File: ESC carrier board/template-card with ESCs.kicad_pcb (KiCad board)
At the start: 2 copper layers, 111.8 x 83 mm, 13 parts, among them J1 Conn_01x10_Pin, J3 Conn_01x04_Pin, J4 Conn_01x04_Pin, J5 Conn_01x04_Pin, SW1 SW_DPDT_x2, U2 ESC, U4 ESC, U6 ESC

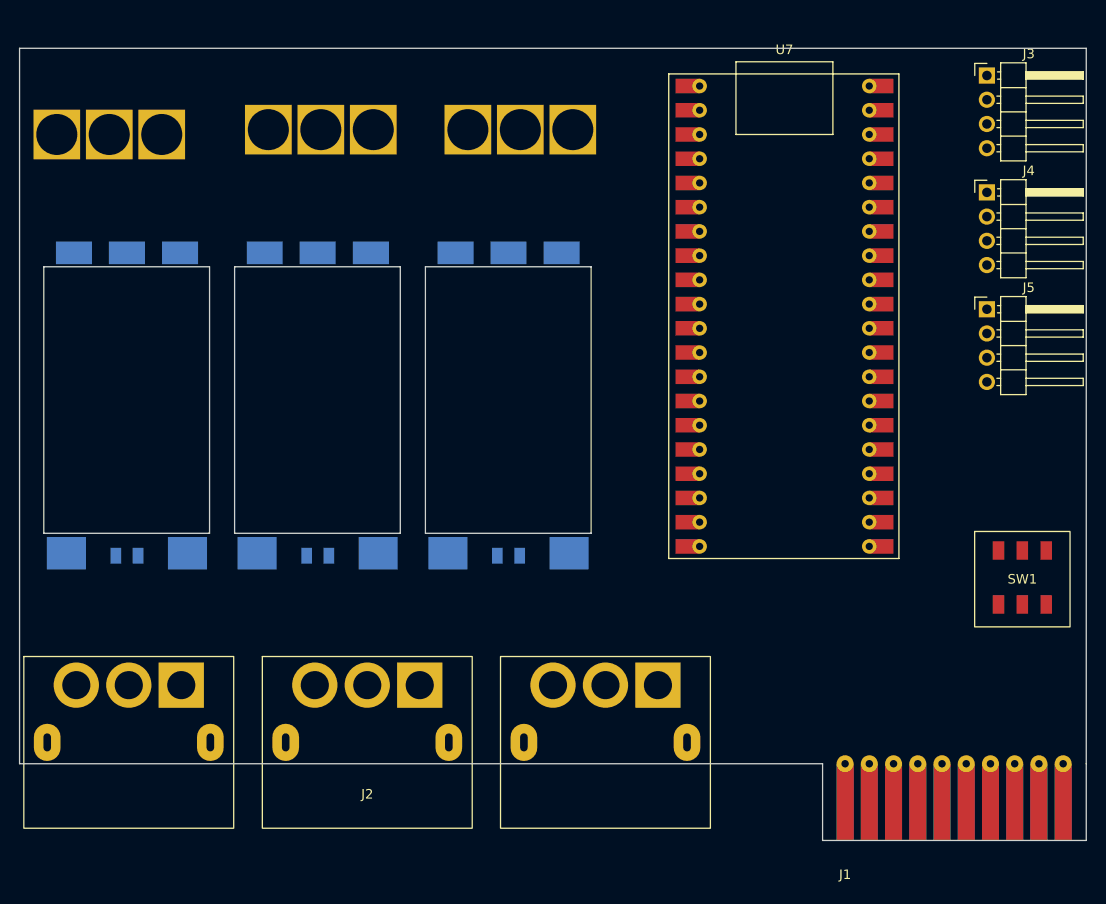
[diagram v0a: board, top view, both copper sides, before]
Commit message: Routed board
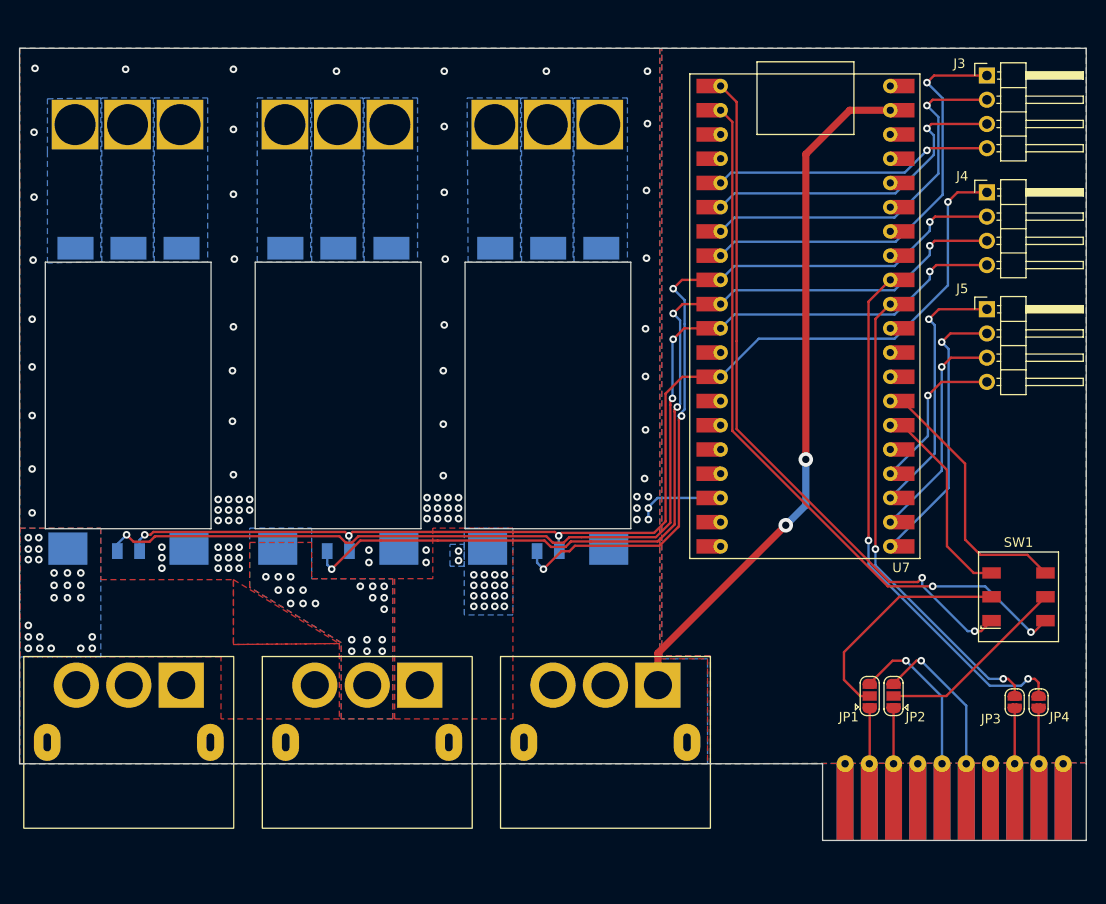
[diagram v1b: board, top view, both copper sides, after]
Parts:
- added JP1: Jumper_3_Open, Jumper:SolderJumper-3_P1.3mm_Open_RoundedPad1.0x1.5mm, F.Cu at (174.8, 92.9)
- added JP2: Jumper_3_Open, Jumper:SolderJumper-3_P1.3mm_Open_RoundedPad1.0x1.5mm, F.Cu at (177.3, 92.9)
- added JP3: Jumper_2_Bridged, Jumper:SolderJumper-2_P1.3mm_Open_RoundedPad1.0x1.5mm, F.Cu at (190.0, 93.5)
- added JP4: Jumper_2_Bridged, Jumper:SolderJumper-2_P1.3mm_Open_RoundedPad1.0x1.5mm, F.Cu at (192.5, 93.5)
- J1: value Conn_01x10_Pin -> ~
- SW1: footprint 2024-backplane:SW_CUI_DPDT -> Kelpie_Default:CUI-Switch-SMD
- U1, U3, U5: footprint ESC-Thruster:MR60-F -> 2024-backplane:MR60-F
- U7: footprint ESC-carrier:ESP32-S3-Pico -> Kelpie_Default:ESP32-S3-Pico
- moved U6 4.19 mm to (132.7, 79.1)
- moved U5 2.87 mm to (141.0, 33.0)
- moved U4 2.21 mm to (110.7, 79.1)
- moved U7 2.20 mm to (169.3, 44.2)
- moved U1 2.18 mm to (97.0, 33.0)
- moved SW1 1.89 mm to (190.4, 82.5), turned to 90 degrees
- moved U3 1.82 mm to (119.0, 33.0)
- moved U2 0.51 mm to (88.7, 79.1)
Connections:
- net GND1 renamed sGND
- J1 pad 2: /tx0/sda0 -> Net-(J1-TX0/SDA0)
- J1 pad 3: /rx0/scl0 -> Net-(J1-RX0/SCL0)
- J1 pad 5: /tx1/sda1 -> Net-(J1-TX1/SDA1)
- J1 pad 6: /rx1/scl1 -> Net-(J1-RX1/SCL1)
- J1 pad 8: /tx2/sda2 -> Net-(J1-TX2/SDA2)
- J1 pad 9: /rx2/scl2 -> Net-(J1-RX2/SCL2)
- J2 pad : (no net) -> GND
- J2 pad 1: /48v -> unconnected-(J2A-48V-Pad1)
- J2 pad 7: /24v -> unconnected-(J2C-24V-Pad7)
- SW1 pad 1: /tx -> TX0
- SW1 pad 2: /tx0/sda0 -> Net-(JP1-C)
- SW1 pad 3: /sda -> SDA0
- SW1 pad 4: /rx -> RX0
- SW1 pad 5: /rx0/scl0 -> Net-(JP2-C)
- SW1 pad 6: /scl -> SCL0
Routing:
- net /sg: track 0.00 -> 120.7 mm, vias 0 -> 4
- net /sGP8: track 0.00 -> 116.0 mm, vias 0 -> 4
- net /sGP7: track 0.00 -> 98.5 mm, vias 0 -> 4
- net /sGP6: track 0.00 -> 79.7 mm, vias 0 -> 4
- net RX0: track 0.00 -> 76.2 mm, vias 0 -> 2
- net TX0: track 0.00 -> 73.5 mm, vias 0 -> 2
- net /5v: track 0.00 -> 72.8 mm, vias 0 -> 2
- net SCL1: track 0.00 -> 55.7 mm, vias 0 -> 2
- net SDA1: track 0.00 -> 48.9 mm, vias 0 -> 2
- net Net-(J3-Pin_1): track 0.00 -> 44.9 mm, vias 0 -> 1
- net Net-(J3-Pin_2): track 0.00 -> 39.5 mm, vias 0 -> 1
- net Net-(J3-Pin_3): track 0.00 -> 34.2 mm, vias 0 -> 1
- net Net-(J3-Pin_4): track 0.00 -> 29.4 mm, vias 0 -> 1
- net Net-(J5-Pin_2): track 0.00 -> 29.4 mm, vias 0 -> 1
- net Net-(J5-Pin_1): track 0.00 -> 27.4 mm, vias 0 -> 1
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- added copper zone on B.Cu, net /12v1
- added copper zone on F.Cu, net /12v1
- added copper zone on B.Cu, net /12v2
- added copper zone on F.Cu, net /12v2
- added copper zone on B.Cu, net /12v3
- added copper zone on F.Cu, net /12v3
- added copper zone on B.Cu, net GND
- added copper zone on F.Cu, net GND
- added copper zone on B.Cu, net Net-(U1-A)
- added copper zone on B.Cu, net Net-(U1-B)
- added copper zone on B.Cu, net Net-(U1-C)
- added copper zone on B.Cu, net Net-(U3-A)
- added copper zone on B.Cu, net Net-(U3-B)
- added copper zone on B.Cu, net Net-(U3-C)
- added copper zone on B.Cu, net Net-(U5-A)
- added copper zone on B.Cu, net Net-(U5-B)
- added copper zone on B.Cu, net Net-(U5-C)
- added copper zone on B.Cu, net sGND
- added copper zone on F.Cu, net sGND
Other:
- outline, holes or cut-outs redrawn

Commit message: Modified board and footprints
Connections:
- J3 pad 1: Net-(J3-Pin_1) -> sGND
- J4 pad 1: /sg -> sGND
- J5 pad 1: Net-(J5-Pin_1) -> sGND
- U2 pad G: /sg -> sGND
- U4 pad G: /sg -> sGND
- U6 pad G: /sg -> sGND
- U7 pad 13: /sg -> sGND
- U7 pad 23: Net-(J5-Pin_1) -> sGND
- U7 pad 28: unconnected-(U7-GND-Pad28) -> sGND
- U7 pad 3: unconnected-(U7-GND-Pad3) -> sGND
- U7 pad 33: unconnected-(U7-GND-Pad33) -> sGND
- U7 pad 38: unconnected-(U7-GND-Pad38) -> sGND
- U7 pad 8: Net-(J3-Pin_1) -> sGND
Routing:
- net /sg: track 120.7 -> 0.00 mm, vias 4 -> 0
- net sGND: track 0.00 -> 79.7 mm, vias 0 -> 43
- net Net-(J3-Pin_1): track 44.9 -> 0.00 mm, vias 1 -> 0
- net Net-(J5-Pin_1): track 27.4 -> 0.00 mm, vias 1 -> 0
- net Net-(J5-Pin_3): track 23.6 -> 24.8 mm
- net Net-(J5-Pin_2): track 29.4 -> 30.2 mm
- added copper zone on F.Cu, net Net-(U1-A)
- added copper zone on F.Cu, net Net-(U1-B)
- added copper zone on F.Cu, net Net-(U1-C)
- added copper zone on F.Cu, net Net-(U3-A)
- added copper zone on F.Cu, net Net-(U3-B)
- added copper zone on F.Cu, net Net-(U3-C)
- added copper zone on F.Cu, net Net-(U5-A)
- added copper zone on F.Cu, net Net-(U5-B)
- added copper zone on F.Cu, net Net-(U5-C)

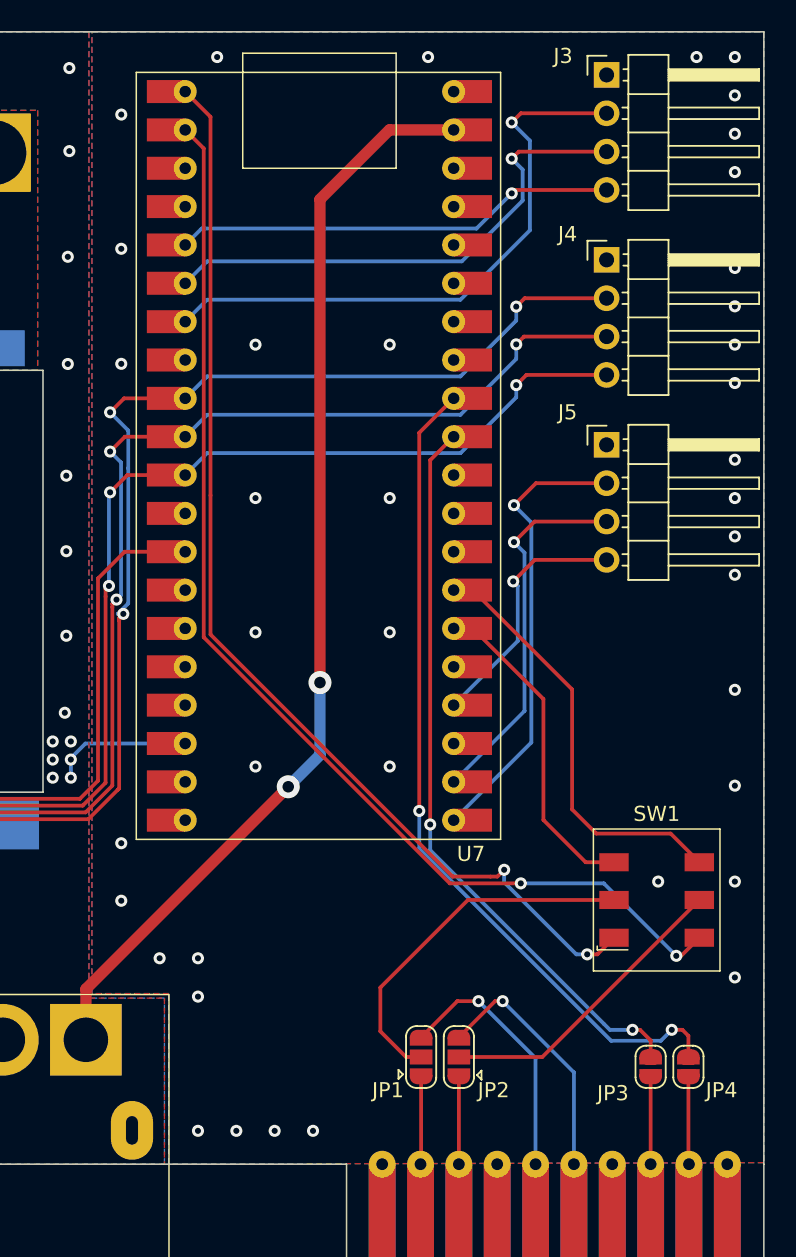
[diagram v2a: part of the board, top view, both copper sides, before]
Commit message: ESC carrier board jumper routing
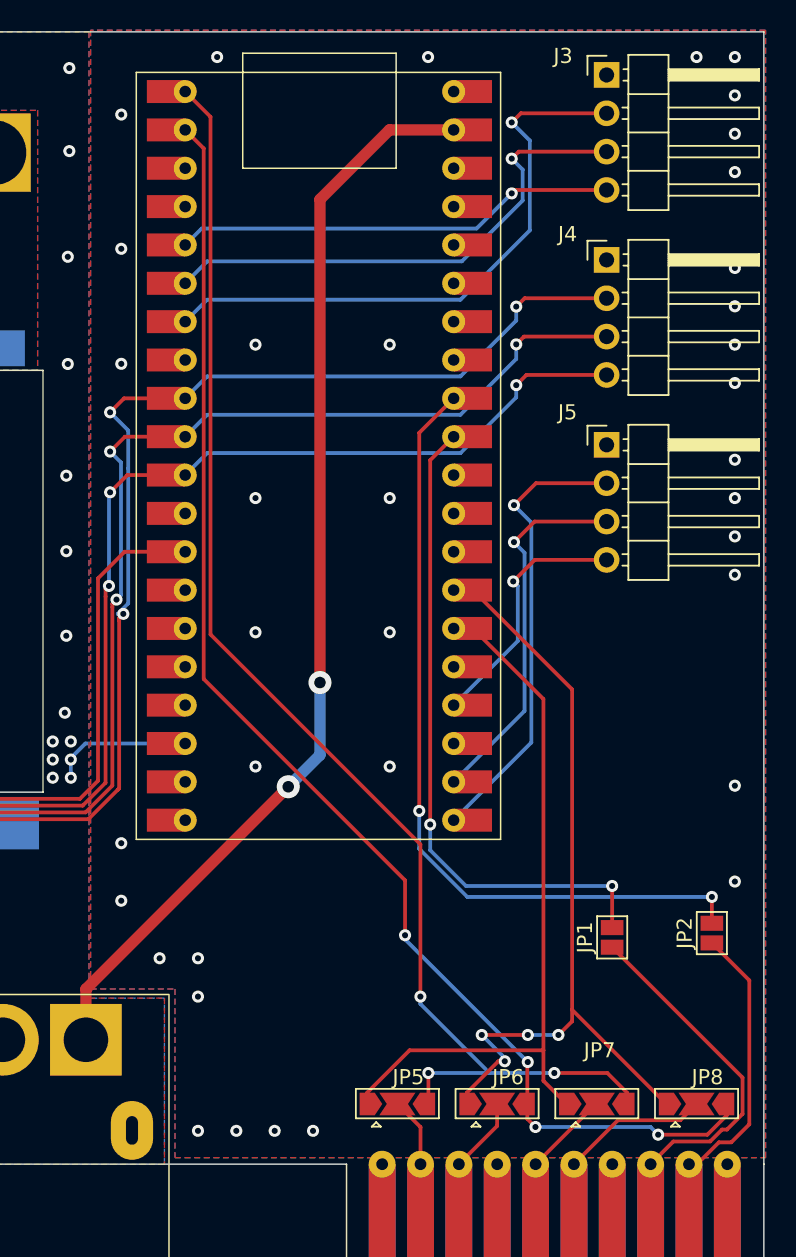
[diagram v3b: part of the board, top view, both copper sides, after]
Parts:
- removed JP3, JP4: Jumper_2_Bridged, Jumper:SolderJumper-2_P1.3mm_Open_RoundedPad1.0x1.5mm
- removed SW1: SW_DPDT_x2, Kelpie_Default:CUI-Switch-SMD
- added JP5: SolderJumper_3_Open, Jumper:SolderJumper-3_P2.0mm_Open_TrianglePad1.0x1.5mm, F.Cu at (173.2, 96.0)
- added JP6: SolderJumper_3_Open, Jumper:SolderJumper-3_P2.0mm_Open_TrianglePad1.0x1.5mm, F.Cu at (179.8, 96.0)
- added JP7: SolderJumper_3_Open, Jumper:SolderJumper-3_P2.0mm_Open_TrianglePad1.0x1.5mm, F.Cu at (186.4, 96.0)
- added JP8: SolderJumper_3_Open, Jumper:SolderJumper-3_P2.0mm_Open_TrianglePad1.0x1.5mm, F.Cu at (193.0, 96.0)
- JP1, JP2: value Jumper_3_Open -> SolderJumper_2_Open; footprint Jumper:SolderJumper-3_P1.3mm_Open_RoundedPad1.0x1.5mm -> Jumper:SolderJumper-2_P1.3mm_Open_Pad1.0x1.5mm
- moved JP2 18.7 mm to (194.1, 84.7)
- moved JP1 14.9 mm to (187.5, 85.0)
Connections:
- J1 pad 2: Net-(J1-TX0/SDA0) -> TX0/SDA0
- J1 pad 3: Net-(J1-RX0/SCL0) -> RX0/SCL0
- J1 pad 5: Net-(J1-TX1/SDA1) -> TX1/SDA1
- J1 pad 6: Net-(J1-RX1/SCL1) -> RX1/SCL1
- JP1 pad 1: Net-(J1-TX0/SDA0) -> Net-(J1-TX2/SDA2)
- JP1 pad 2: Net-(JP1-C) -> SDA1
- JP2 pad 1: Net-(J1-RX0/SCL0) -> Net-(J1-RX2/SCL2)
- JP2 pad 2: Net-(JP2-C) -> SCL1
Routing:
- net SDA0: track 20.5 -> 47.7 mm
- net SCL0: track 27.1 -> 53.0 mm, vias 0 -> 4
- net Net-(JP1-C): track 24.2 -> 0.00 mm
- net Net-(JP2-C): track 20.2 -> 0.00 mm
- net Net-(J1-TX1/SDA1): track 17.2 -> 0.00 mm, vias 1 -> 0
- net Net-(J1-RX1/SCL1): track 16.6 -> 0.00 mm, vias 1 -> 0
- net TX0: track 73.5 -> 89.9 mm, vias 2 -> 3
- net Net-(J1-TX2/SDA2): track 5.80 -> 22.1 mm
- net RX0: track 76.2 -> 89.8 mm, vias 2 -> 4
- net Net-(J1-RX2/SCL2): track 5.82 -> 18.6 mm
- net RX1/SCL1: track 0.00 -> 9.77 mm
- net Net-(J1-TX0/SDA0): track 5.82 -> 0.00 mm
- net Net-(J1-RX0/SCL0): track 5.80 -> 0.00 mm
- net TX1/SDA1: track 0.00 -> 5.71 mm
- net SDA1: track 48.9 -> 43.8 mm
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
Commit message: modified pcb
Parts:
- moved JP8 10.2 mm to (187.3, 87.6)
- moved JP1 8.89 mm to (190.5, 93.3)
- moved JP6 8.80 mm to (177.2, 87.6)
- moved JP2 8.70 mm to (193.0, 93.3)
- moved JP7 5.34 mm to (182.2, 92.7)
- moved JP5 3.53 mm to (172.0, 92.7)
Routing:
- net sGND: track 79.7 -> 97.7 mm, vias 40 -> 41
- net Net-(J1-TX2/SDA2): track 22.1 -> 6.75 mm
- net RX0: track 89.8 -> 76.3 mm, vias 4 -> 0
- net SCL0: track 53.0 -> 41.5 mm, vias 4 -> 3
- net Net-(J1-RX2/SCL2): track 18.6 -> 8.21 mm
- net RX0/SCL0: track 5.04 -> 12.4 mm
- net SDA1: track 43.8 -> 48.0 mm, vias 2 -> 0
- net SDA0: track 47.7 -> 43.7 mm, vias 0 -> 3
- net TX0/SDA0: track 4.68 -> 8.49 mm
- net TX0: track 89.9 -> 86.2 mm, vias 3 -> 2
- net SCL1: track 53.2 -> 49.5 mm, vias 2 -> 0
- net RX1/SCL1: track 9.77 -> 13.3 mm
- net TX1/SDA1: track 5.71 -> 7.35 mm
- net Net-(U5-C): vias 0 -> 6
- net Net-(U5-B): vias 0 -> 6
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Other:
- board text added: "0"
- board text added: "1"
- board text added: "2"
- board text added: "RX"
- board text added: "SCL"
- board text added: "SCL1"
- board text added: "SDA"
- board text added: "SDA1"
- board text added: "TX"

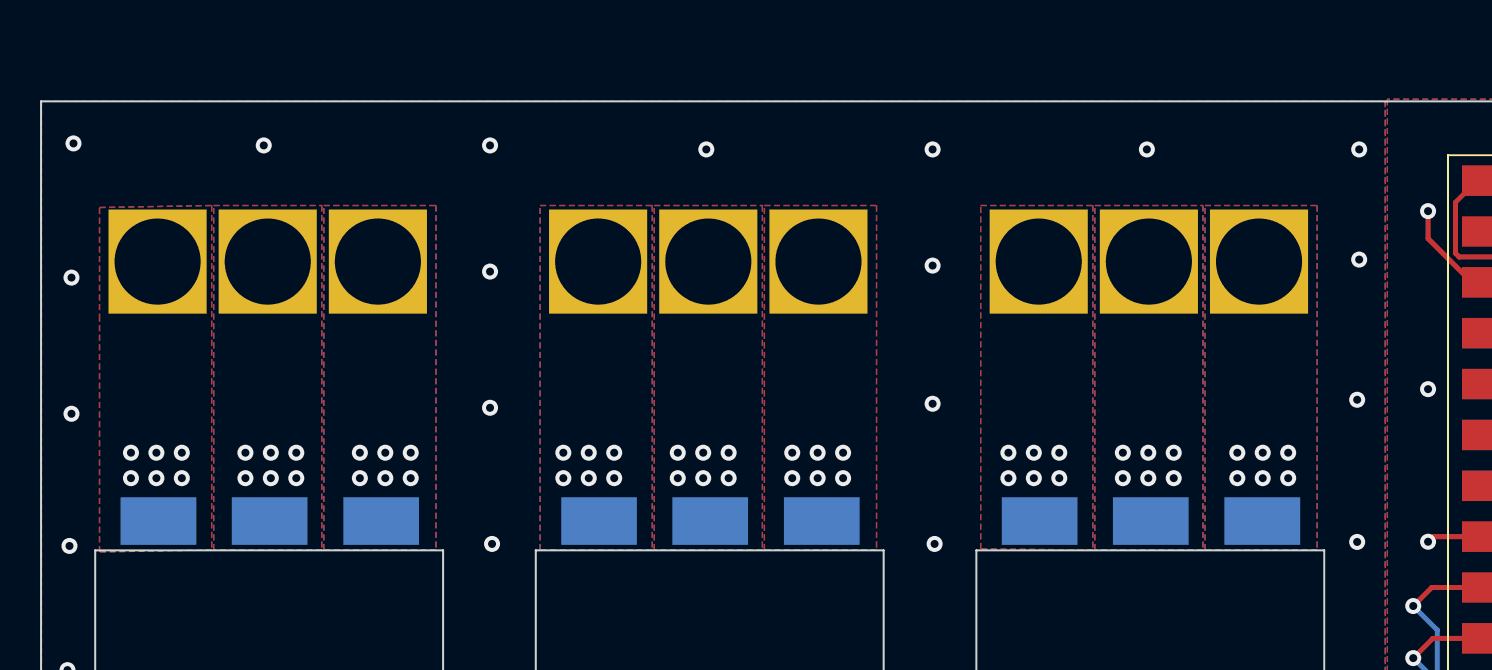
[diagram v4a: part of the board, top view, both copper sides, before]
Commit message: changed to mr60PW-M connector
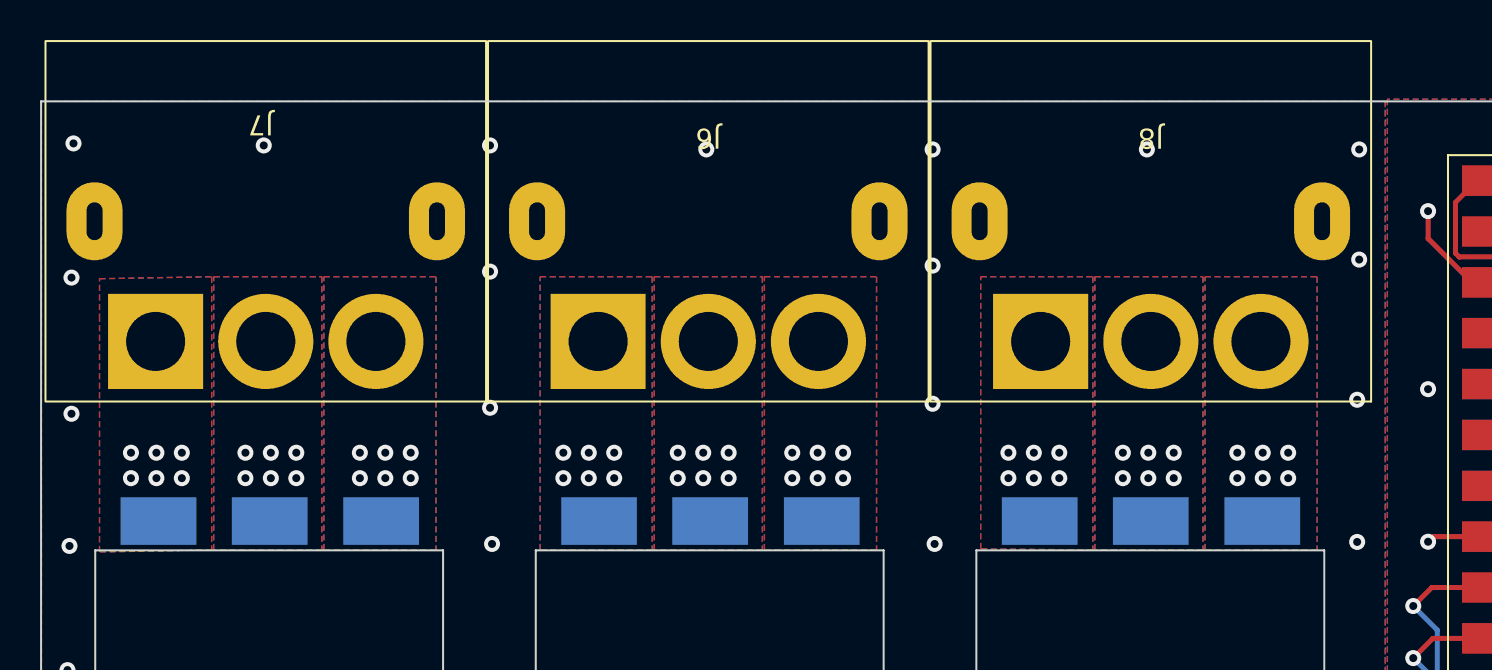
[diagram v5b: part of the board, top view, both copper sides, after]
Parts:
- removed U1, U3, U5: ~, 2024-backplane:MR60-F
- added J6: ~, 2024-backplane:MR60PW-M, F.Cu at (119.0, 37.0)
- added J7: ~, 2024-backplane:MR60PW-M, F.Cu at (96.9, 37.0)
- added J8: ~, 2024-backplane:MR60PW-M, F.Cu at (141.1, 37.0)
